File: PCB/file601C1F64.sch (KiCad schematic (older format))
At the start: 4 parts, among them IC7 DS3231MZ_V+, U2 103

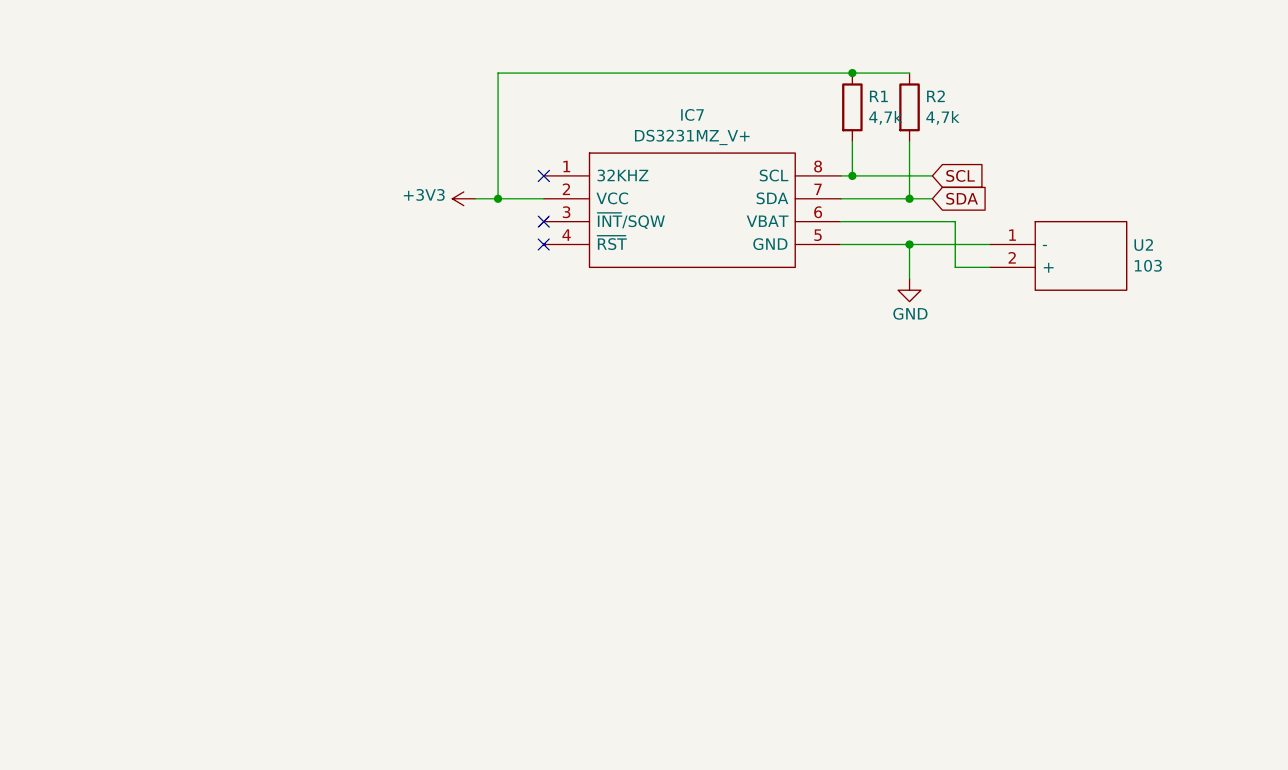
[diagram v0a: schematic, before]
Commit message: Cleaned up repository. Created a BOM in iBOM Format.
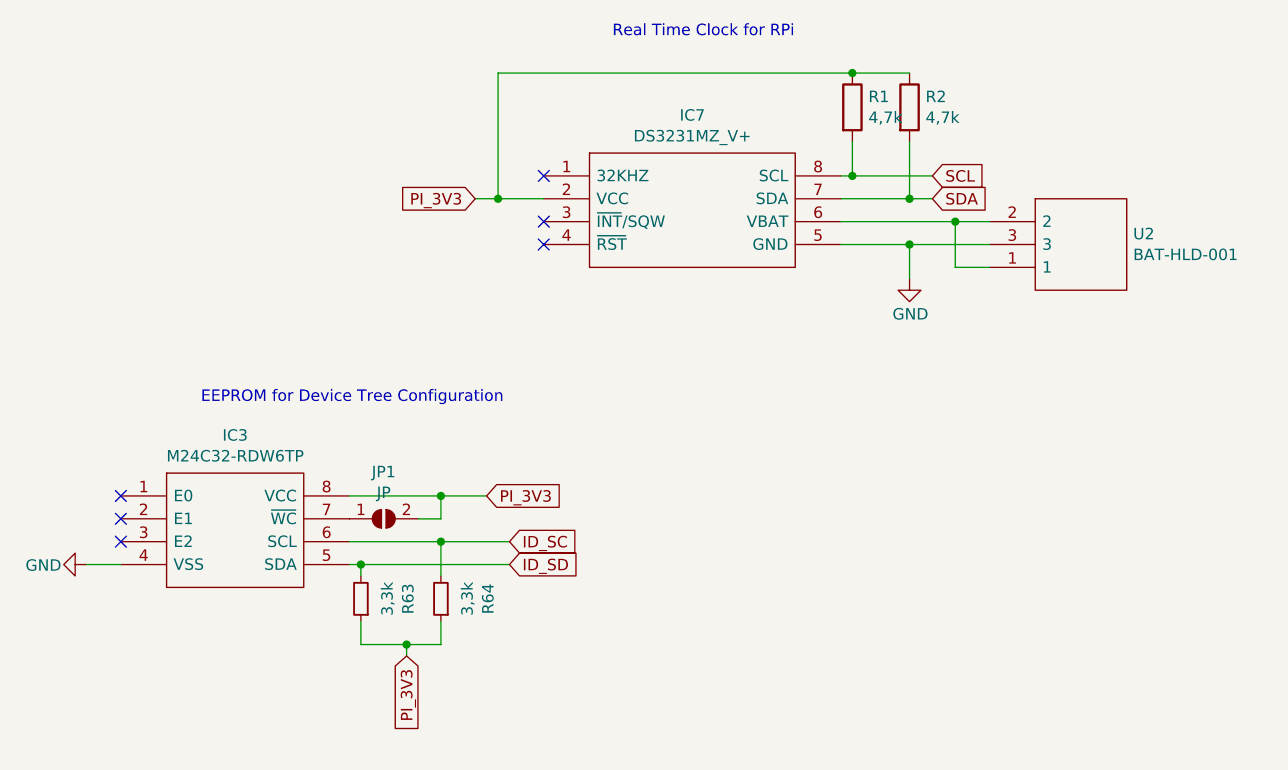
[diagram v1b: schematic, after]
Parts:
- removed U2: 103, 103, symbol SamacSys_Parts:103
- added IC3: M24C32-RDW6TP, SOP65P640X120-8N, symbol SamacSys_Parts:M24C32-RDW6TP
- added JP1: JP, Jumper:SolderJumper-2_P1.3mm_Open_RoundedPad1.0x1.5mm, symbol Jumper:SolderJumper_2_Open
- added R63, R64: 3,3k, Resistor_SMD:R_0805_2012Metric_Pad1.15x1.40mm_HandSolder, symbol Device:R_Small
- added U2: BAT-HLD-001, BATHLD001, symbol SamacSys_Parts:BAT-HLD-001
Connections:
- net GND: now also IC3.4 (VSS), U2.3
- net at IC7.6 (VBAT): now also U2.1, U2.2
- net +3V3 renamed PI_3V3
- net PI_3V3: now also IC3.8 (VCC), JP1.2 (B), R63.1, R64.1
- new net: IC3.7 (~WC), JP1.1 (A)
- new net ID_SC: IC3.6 (SCL), R64.2
- new net ID_SD: IC3.5 (SDA), R63.2
- no-connect marks 3 -> 6
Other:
- note added: "EEPROM for Device Tree Configuration"
- note added: "Real Time Clock for RPi"
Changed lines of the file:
@@
-$EndComp
-$Comp
-L power:+3V3 #PWR?
-U 1 1 601C966A
-P 4050 3200
-AR Path="/601C966A" Ref="#PWR?"  Part="1"
-AR Path="/601C1F65/601C966A" Ref="#PWR0102"  Part="1"
-F 0 "#PWR0102" H 4050 3050 50  0001 C CNN
-F 1 "+3V3" V 4065 3328 50  0000 L CNN
-F 2 "" H 4050 3200 50  0001 C CNN
-F 3 "" H 4050 3200 50  0001 C CNN
-	1    4050 3200
-	0    -1   -1   0
 $EndComp
 $Comp
@@
 Wire Wire Line
 	5950 3400 5650 3400
-$Comp
-L SamacSys_Parts:103 U?
-U 1 1 601C96A2
-P 6300 3400
-AR Path="/601C96A2" Ref="U?"  Part="1"
-AR Path="/601C1F65/601C96A2" Ref="U2"  Part="1"
-F 0 "U2" H 6928 3396 50  0000 L CNN
-F 1 "103" H 6928 3305 50  0000 L CNN
-F 2 "103" H 6950 3500 50  0001 L CNN
-F 3 "http://www.keyelco.com/product-pdf.cfm?p=719" H 6950 3400 50  0001 L CNN
-F 4 "KEYSTONE - 103 - BATTERY HOLDER, 20MM COIN CELL, SMD" H 6950 3300 50  0001 L CNN "Description"
-F 5 "" H 6950 3200 50  0001 L CNN "Height"
-F 6 "534-103" H 6950 3100 50  0001 L CNN "Mouser Part Number"
-F 7 "https://www.mouser.co.uk/ProductDetail/Keystone-Electronics/103?qs=Q3RoVmURDolsdXuDGYj49g%3D%3D" H 6950 3000 50  0001 L CNN "Mouser Price/Stock"
-F 8 "Keystone Electronics" H 6950 2900 50  0001 L CNN "Manufacturer_Name"
-F 9 "103" H 6950 2800 50  0001 L CNN "Manufacturer_Part_Number"
-	1    6300 3400
-	1    0    0    -1
-$EndComp
 Wire Wire Line
 	6300 3400 5950 3400
@@
 Wire Wire Line
 	6150 3500 6300 3500
+$Comp
+L SamacSys_Parts:M24C32-RDW6TP IC?
+U 1 1 60335062
+P 2500 4500
+AR Path="/60335062" Ref="IC?"  Part="1"
+AR Path="/601C1F65/60335062" Ref="IC3"  Part="1"
+F 0 "IC3" H 3000 4765 50  0000 C CNN
+F 1 "M24C32-RDW6TP" H 3000 4674 50  0000 C CNN
+F 2 "SOP65P640X120-8N" H 3350 4600 50  0001 L CNN
+F 3 "http://www.st.com/content/ccc/resource/technical/document/datasheet/80/4e/8c/54/f2/63/4c/4a/CD00001012.pdf/files/CD00001012.pdf/jcr:content/translations/en.CD00001012.pdf" H 3350 4500 50  0001 L CNN
+F 4 "STMICROELECTRONICS - M24C32-RDW6TP - EEPROM, 32KBIT, I2C, 1MHZ, TSSOP-8" H 3350 4400 50  0001 L CNN "Description"
+F 5 "1.2" H 3350 4300 50  0001 L CNN "Height"
+F 6 "511-M24C32-RDW6TP" H 3350 4200 50  0001 L CNN "Mouser Part Number"
+F 7 "https://www.mouser.co.uk/ProductDetail/STMicroelectronics/M24C32-RDW6TP/?qs=%252B9pWl1iD4MVhMVBjnj8NEA%3D%3D" H 3350 4100 50  0001 L CNN "Mouser Price/Stock"
+F 8 "STMicroelectronics" H 3350 4000 50  0001 L CNN "Manufacturer_Name"
+F 9 "M24C32-RDW6TP" H 3350 3900 50  0001 L CNN "Manufacturer_Part_Number"
+	1    2500 4500
+	1    0    0    -1
+$EndComp
+$Comp
+L power:GND #PWR0144
+U 1 1 6033506E
+P 2350 4800
+F 0 "#PWR0144" H 2350 4550 50  0001 C CNN
+F 1 "GND" V 2354 4690 50  0000 R CNN
+F 2 "" H 2350 4800 50  0001 C CNN
+F 3 "" H 2350 4800 50  0001 C CNN
+	1    2350 4800
+	0    1    1    0
+$EndComp
+Wire Wire Line
+	2350 4800 2500 4800
+Text GLabel 4200 4800 2    50   Input ~ 0
+ID_SD
+Text GLabel 4200 4700 2    50   Input ~ 0
+ID_SC
+$Comp
+L Jumper:SolderJumper_2_Open JP?
+U 1 1 60335077
+P 3650 4600
+AR Path="/60335077" Ref="JP?"  Part="1"
+AR Path="/601C1F65/60335077" Ref="JP1"  Part="1"
+F 0 "JP1" H 3650 4805 50  0000 C CNN
+F 1 "JP" H 3650 4714 50  0000 C CNN
+F 2 "Jumper:SolderJumper-2_P1.3mm_Open_RoundedPad1.0x1.5mm" H 3650 4600 50  0001 C CNN
+F 3 "~" H 3650 4600 50  0001 C CNN
+	1    3650 4600
+	1    0    0    -1
+$EndComp
+Wire Wire Line
+	3500 4500 3900 4500
+Wire Wire Line
+	3800 4600 3900 4600
+Wire Wire Line
+	3900 4600 3900 4500
+Connection ~ 3900 4500
+Wire Wire Line
+	3900 4500 4100 4500
+Wire Wire Line
+	3500 4700 3900 4700
+Wire Wire Line
+	3500 4800 3550 4800
+$Comp
+L Device:R_Small R?
+U 1 1 60335084
+P 3550 4950
+AR Path="/60335084" Ref="R?"  Part="1"
+AR Path="/601C1F65/60335084" Ref="R63"  Part="1"
+F 0 "R63" V 3343 4950 50  0000 C CNN
+F 1 "3,3k" V 3434 4950 50  0000 C CNN
+F 2 "Resistor_SMD:R_0805_2012Metric_Pad1.15x1.40mm_HandSolder" V 3480 4950 50  0001 C CNN
+F 3 "~" H 3550 4950 50  0001 C CNN
+	1    3550 4950
+	-1   0    0    1
+$EndComp
+Connection ~ 3550 4800
+Wire Wire Line
+	3550 4800 4200 4800
+$Comp
+L Device:R_Small R?
+U 1 1 6033508C
+P 3900 4950
+AR Path="/6033508C" Ref="R?"  Part="1"
+AR Path="/601C1F65/6033508C" Ref="R64"  Part="1"
+F 0 "R64" V 3693 4950 50  0000 C CNN
+F 1 "3,3k" V 3784 4950 50  0000 C CNN
+F 2 "Resistor_SMD:R_0805_2012Metric_Pad1.15x1.40mm_HandSolder" V 3830 4950 50  0001 C CNN
+F 3 "~" H 3900 4950 50  0001 C CNN
+	1    3900 4950
+	-1   0    0    1
+$EndComp
+Wire Wire Line
+	3900 4850 3900 4700
+Connection ~ 3900 4700
+Wire Wire Line
+	3900 4700 4200 4700
+Wire Wire Line
+	3550 4850 3550 4800
+Wire Wire Line
+	3900 5050 3900 5150
+Wire Wire Line
+	3550 5050 3550 5150
+NoConn ~ 2500 4500
+NoConn ~ 2500 4600
+NoConn ~ 2500 4700
+Text Notes 2850 4100 0    50   ~ 0
+EEPROM for Device Tree Configuration
+Text Notes 4650 2500 0    50   ~ 0
+Real Time Clock for RPi
+Text GLabel 4050 3200 0    50   Input ~ 0
+PI_3V3
+Text GLabel 4100 4500 2    50   Input ~ 0
+PI_3V3
+Wire Wire Line
+	3550 5150 3750 5150
+Text GLabel 3750 5200 3    50   Input ~ 0
+PI_3V3
+Wire Wire Line
+	3750 5200 3750 5150
+Connection ~ 3750 5150
+Wire Wire Line
+	3750 5150 3900 5150
+$Comp
+L SamacSys_Parts:BAT-HLD-001 U2
+U 1 1 60614704
+P 6300 3300
+F 0 "U2" H 6928 3246 50  0000 L CNN
+F 1 "BAT-HLD-001" H 6928 3155 50  0000 L CNN
+F 2 "BATHLD001" H 6950 3400 50  0001 L CNN
+F 3 "" H 6950 3300 50  0001 L CNN
+F 4 "Coin Cell Battery Holders Linx CR2032 Battery Holder" H 6950 3200 50  0001 L CNN "Description"
+F 5 "4" H 6950 3100 50  0001 L CNN "Height"
+F 6 "712-BAT-HLD-001" H 6950 3000 50  0001 L CNN "Mouser Part Number"
+F 7 "https://www.mouser.co.uk/ProductDetail/Linx-Technologies/BAT-HLD-001/?qs=K5ta8V%252BWhta7hbVGfm4dqA%3D%3D" H 6950 2900 50  0001 L CNN "Mouser Price/Stock"
+F 8 "Linx Technologies" H 6950 2800 50  0001 L CNN "Manufacturer_Name"
+F 9 "BAT-HLD-001" H 6950 2700 50  0001 L CNN "Manufacturer_Part_Number"
+	1    6300 3300
+	1    0    0    -1
+$EndComp
+Wire Wire Line
+	6150 3300 6300 3300
+Connection ~ 6150 3300
 $EndSCHEMATC

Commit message: Completed parts details on schematics and recreated gerbers and bom.
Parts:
- IC3: LCSC (none) -> C283444
- IC7: LCSC (none) -> C107410
- R1, R2: LCSC (none) -> C61924; Manufacturer_Name (none) -> Vishay; Manufacturer_Part_Number (none) -> CRCW08054K70FKEAC; Mouser Part Number (none) -> 71-CRCW08054K70FKEAC; Mouser Price/Stock (none) -> https://www.mouser.de/ProductDetail/Vishay-Dale/CRCW08054K7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
- R63, R64: LCSC (none) -> C26010; Manufacturer_Name (none) -> Vishay; Manufacturer_Part_Number (none) -> CRCW08053K30FKEAC; Mouser Part Number (none) -> 71-CRCW08053K30FKEAC
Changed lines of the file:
@@
 F 2 "Resistor_SMD:R_0805_2012Metric_Pad1.15x1.40mm_HandSolder" V 5630 2800 50  0001 C CNN
 F 3 "~" H 5700 2800 50  0001 C CNN
+F 4 "C61924" H 5700 2800 50  0001 C CNN "LCSC"
+F 5 "Vishay" H 5700 2800 50  0001 C CNN "Manufacturer_Name"
+F 6 "CRCW08054K70FKEAC" H 5700 2800 50  0001 C CNN "Manufacturer_Part_Number"
+F 7 "71-CRCW08054K70FKEAC" H 5700 2800 50  0001 C CNN "Mouser Part Number"
+F 8 "https://www.mouser.de/ProductDetail/Vishay-Dale/CRCW08054K70FKEAC/?qs=%2Fha2pyFaduhkDOWkOJXWlCr7OW2P617rEYihhYtlcgqIKvjKQ0DWSVxd3tufRT70" H 5700 2800 50  0001 C CNN "Mouser Price/Stock"
 	1    5700 2800
 	1    0    0    -1
@@
 F 2 "Resistor_SMD:R_0805_2012Metric_Pad1.15x1.40mm_HandSolder" V 5880 2800 50  0001 C CNN
 F 3 "~" H 5950 2800 50  0001 C CNN
+F 4 "C61924" H 5950 2800 50  0001 C CNN "LCSC"
+F 5 "Vishay" H 5950 2800 50  0001 C CNN "Manufacturer_Name"
+F 6 "CRCW08054K70FKEAC" H 5950 2800 50  0001 C CNN "Manufacturer_Part_Number"
+F 7 "71-CRCW08054K70FKEAC" H 5950 2800 50  0001 C CNN "Mouser Part Number"
+F 8 "https://www.mouser.de/ProductDetail/Vishay-Dale/CRCW08054K70FKEAC/?qs=%2Fha2pyFaduhkDOWkOJXWlCr7OW2P617rEYihhYtlcgqIKvjKQ0DWSVxd3tufRT70" H 5950 2800 50  0001 C CNN "Mouser Price/Stock"
 	1    5950 2800
 	1    0    0    -1
@@
 F 8 "Maxim Integrated" H 5500 2600 50  0001 L CNN "Manufacturer_Name"
 F 9 "DS3231MZ/V+" H 5500 2500 50  0001 L CNN "Manufacturer_Part_Number"
+F 10 "C107410" H 4350 3100 50  0001 C CNN "LCSC"
 	1    4350 3100
 	1    0    0    -1
@@
 F 8 "STMicroelectronics" H 3350 4000 50  0001 L CNN "Manufacturer_Name"
 F 9 "M24C32-RDW6TP" H 3350 3900 50  0001 L CNN "Manufacturer_Part_Number"
+F 10 "C283444" H 2500 4500 50  0001 C CNN "LCSC"
 	1    2500 4500
 	1    0    0    -1
@@
 F 2 "Resistor_SMD:R_0805_2012Metric_Pad1.15x1.40mm_HandSolder" V 3480 4950 50  0001 C CNN
 F 3 "~" H 3550 4950 50  0001 C CNN
+F 4 "C26010" H 3550 4950 50  0001 C CNN "LCSC"
+F 5 "Vishay" H 3550 4950 50  0001 C CNN "Manufacturer_Name"
+F 6 "CRCW08053K30FKEAC" H 3550 4950 50  0001 C CNN "Manufacturer_Part_Number"
+F 7 "71-CRCW08053K30FKEAC" H 3550 4950 50  0001 C CNN "Mouser Part Number"
 	1    3550 4950
 	-1   0    0    1
@@
 F 2 "Resistor_SMD:R_0805_2012Metric_Pad1.15x1.40mm_HandSolder" V 3830 4950 50  0001 C CNN
 F 3 "~" H 3900 4950 50  0001 C CNN
+F 4 "C26010" H 3900 4950 50  0001 C CNN "LCSC"
+F 5 "Vishay" H 3900 4950 50  0001 C CNN "Manufacturer_Name"
+F 6 "CRCW08053K30FKEAC" H 3900 4950 50  0001 C CNN "Manufacturer_Part_Number"
+F 7 "71-CRCW08053K30FKEAC" H 3900 4950 50  0001 C CNN "Mouser Part Number"
 	1    3900 4950
 	-1   0    0    1

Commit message: Refactored JLC Part Numbers. And replaced 100uF capacitors with 1206 sized parts.
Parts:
- IC3: LCSC C283444 -> (none)
- IC7: LCSC C107410 -> (none)
- R1, R2: LCSC C61924 -> C17673
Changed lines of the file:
@@
 F 2 "Resistor_SMD:R_0805_2012Metric_Pad1.15x1.40mm_HandSolder" V 5630 2800 50  0001 C CNN
 F 3 "~" H 5700 2800 50  0001 C CNN
-F 4 "C61924" H 5700 2800 50  0001 C CNN "LCSC"
+F 4 "C17673" H 5700 2800 50  0001 C CNN "LCSC"
 F 5 "Vishay" H 5700 2800 50  0001 C CNN "Manufacturer_Name"
 F 6 "CRCW08054K70FKEAC" H 5700 2800 50  0001 C CNN "Manufacturer_Part_Number"
@@
 F 2 "Resistor_SMD:R_0805_2012Metric_Pad1.15x1.40mm_HandSolder" V 5880 2800 50  0001 C CNN
 F 3 "~" H 5950 2800 50  0001 C CNN
-F 4 "C61924" H 5950 2800 50  0001 C CNN "LCSC"
+F 4 "C17673" H 5950 2800 50  0001 C CNN "LCSC"
 F 5 "Vishay" H 5950 2800 50  0001 C CNN "Manufacturer_Name"
 F 6 "CRCW08054K70FKEAC" H 5950 2800 50  0001 C CNN "Manufacturer_Part_Number"
@@
 F 8 "Maxim Integrated" H 5500 2600 50  0001 L CNN "Manufacturer_Name"
 F 9 "DS3231MZ/V+" H 5500 2500 50  0001 L CNN "Manufacturer_Part_Number"
-F 10 "C107410" H 4350 3100 50  0001 C CNN "LCSC"
+F 10 "" H 4350 3100 50  0001 C CNN "LCSC"
 	1    4350 3100
 	1    0    0    -1
@@
 F 8 "STMicroelectronics" H 3350 4000 50  0001 L CNN "Manufacturer_Name"
 F 9 "M24C32-RDW6TP" H 3350 3900 50  0001 L CNN "Manufacturer_Part_Number"
-F 10 "C283444" H 2500 4500 50  0001 C CNN "LCSC"
+F 10 "" H 2500 4500 50  0001 C CNN "LCSC"
 	1    2500 4500
 	1    0    0    -1
